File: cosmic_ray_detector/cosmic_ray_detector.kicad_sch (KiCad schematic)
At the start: 0 parts

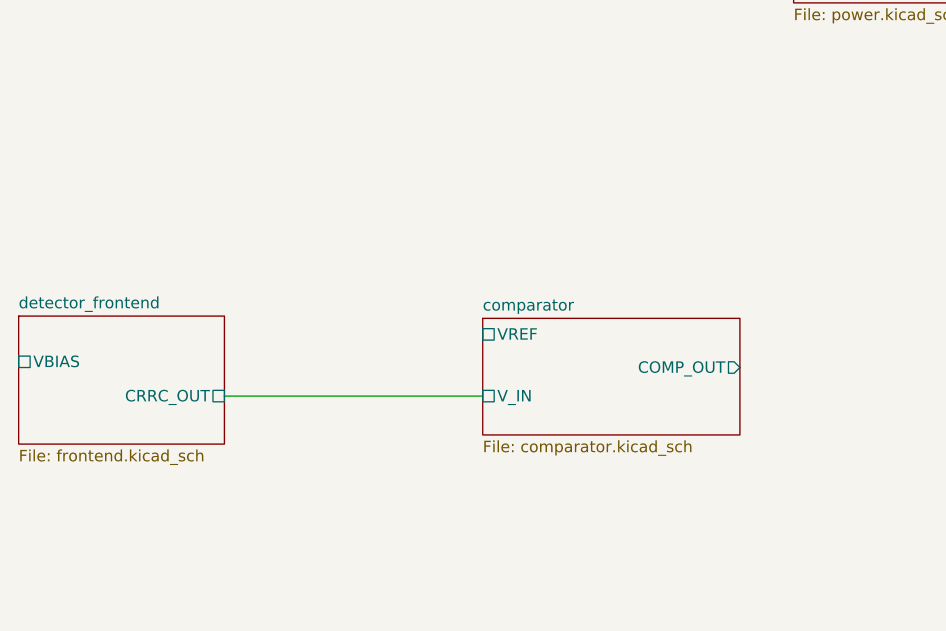
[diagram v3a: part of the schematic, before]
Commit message: schematic for threshold setting
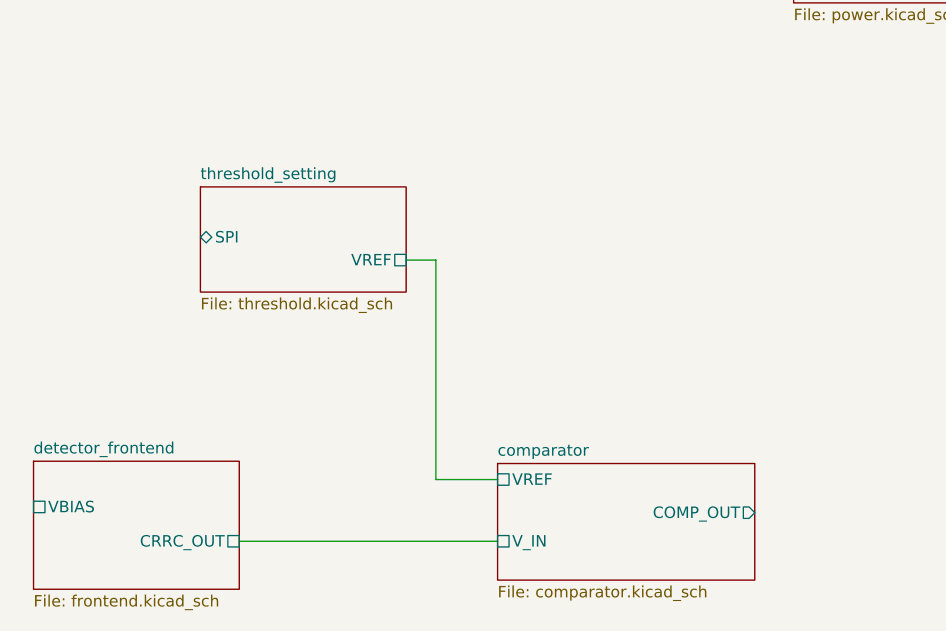
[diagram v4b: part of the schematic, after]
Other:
- added sheet threshold_setting (threshold.kicad_sch)
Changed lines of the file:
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@@
     (comment 1 "design by: Dan Weatherill")
   )
-  (wire (pts (xy 117.094 85.598) (xy 145.796 85.598))
-    (stroke (width 0) (type default) (color 0 0 0 0))
-  )
-  (sheet (at 94.234 76.708) (size 22.86 14.224) (fields_autoplaced)
-    (stroke (width 0.1524) (type solid) (color 0 0 0 0))
-    (fill (color 0 0 0 0.0000))
-    (property "Sheet name" "detector_frontend" (id 0) (at 94.234 75.9964 0)
-      (effects (font (size 1.27 1.27)) (justify left bottom))
-    )
-    (property "Sheet file" "frontend.kicad_sch" (id 1) (at 94.234 91.5166 0)
-      (effects (font (size 1.27 1.27)) (justify left top))
-    )
-    (pin "VBIAS" passive (at 94.234 81.788 180)
-      (effects (font (size 1.27 1.27)) (justify left))
-    )
-    (pin "CRRC_OUT" passive (at 117.094 85.598 0)
+  (wire (pts (xy 140.589 94.869) (xy 147.447 94.869))
+    (stroke (width 0) (type default) (color 0 0 0 0))
+  )
+  (wire (pts (xy 137.287 70.485) (xy 140.589 70.485))
+    (stroke (width 0) (type default) (color 0 0 0 0))
+  )
+  (wire (pts (xy 140.589 70.485) (xy 140.589 94.869))
+    (stroke (width 0) (type default) (color 0 0 0 0))
+  )
+  (wire (pts (xy 118.745 101.727) (xy 147.447 101.727))
+    (stroke (width 0) (type default) (color 0 0 0 0))
+  )
+  (sheet (at 114.427 62.357) (size 22.86 11.684) (fields_autoplaced)
+    (stroke (width 0.1524) (type solid) (color 0 0 0 0))
+    (fill (color 0 0 0 0.0000))
+    (property "Sheet name" "threshold_setting" (id 0) (at 114.427 61.6454 0)
+      (effects (font (size 1.27 1.27)) (justify left bottom))
+    )
+    (property "Sheet file" "threshold.kicad_sch" (id 1) (at 114.427 74.6256 0)
+      (effects (font (size 1.27 1.27)) (justify left top))
+    )
+    (pin "SPI" bidirectional (at 114.427 67.945 180)
+      (effects (font (size 1.27 1.27)) (justify left))
+    )
+    (pin "VREF" passive (at 137.287 70.485 0)
       (effects (font (size 1.27 1.27)) (justify right))
     )
   )
-  (sheet (at 145.796 76.962) (size 28.575 12.954) (fields_autoplaced)
-    (stroke (width 0.1524) (type solid) (color 0 0 0 0))
-    (fill (color 0 0 0 0.0000))
-    (property "Sheet name" "comparator" (id 0) (at 145.796 76.2504 0)
-      (effects (font (size 1.27 1.27)) (justify left bottom))
-    )
-    (property "Sheet file" "comparator.kicad_sch" (id 1) (at 145.796 90.5006 0)
-      (effects (font (size 1.27 1.27)) (justify left top))
-    )
-    (pin "V_IN" passive (at 145.796 85.598 180)
-      (effects (font (size 1.27 1.27)) (justify left))
-    )
-    (pin "VREF" passive (at 145.796 78.74 180)
-      (effects (font (size 1.27 1.27)) (justify left))
-    )
-    (pin "COMP_OUT" output (at 174.371 82.423 0)
+  (sheet (at 95.885 92.837) (size 22.86 14.224) (fields_autoplaced)
+    (stroke (width 0.1524) (type solid) (color 0 0 0 0))
+    (fill (color 0 0 0 0.0000))
+    (property "Sheet name" "detector_frontend" (id 0) (at 95.885 92.1254 0)
+      (effects (font (size 1.27 1.27)) (justify left bottom))
+    )
+    (property "Sheet file" "frontend.kicad_sch" (id 1) (at 95.885 107.6456 0)
+      (effects (font (size 1.27 1.27)) (justify left top))
+    )
+    (pin "VBIAS" passive (at 95.885 97.917 180)
+      (effects (font (size 1.27 1.27)) (justify left))
+    )
+    (pin "CRRC_OUT" passive (at 118.745 101.727 0)
+      (effects (font (size 1.27 1.27)) (justify right))
+    )
+  )
+  (sheet (at 147.447 93.091) (size 28.575 12.954) (fields_autoplaced)
+    (stroke (width 0.1524) (type solid) (color 0 0 0 0))
+    (fill (color 0 0 0 0.0000))
+    (property "Sheet name" "comparator" (id 0) (at 147.447 92.3794 0)
+      (effects (font (size 1.27 1.27)) (justify left bottom))
+    )
+    (property "Sheet file" "comparator.kicad_sch" (id 1) (at 147.447 106.6296 0)
+      (effects (font (size 1.27 1.27)) (justify left top))
+    )
+    (pin "V_IN" passive (at 147.447 101.727 180)
+      (effects (font (size 1.27 1.27)) (justify left))
+    )
+    (pin "VREF" passive (at 147.447 94.869 180)
+      (effects (font (size 1.27 1.27)) (justify left))
+    )
+    (pin "COMP_OUT" output (at 176.022 98.552 0)
       (effects (font (size 1.27 1.27)) (justify right))
     )
@@
     (path "/a7a79d2b-04f1-477d-ba1e-3ead0da72cb2" (page "3"))
     (path "/86d8b01b-5c34-47c3-904c-67d3d9a70426" (page "4"))
+    (path "/5d423df9-0691-4d6c-a6f8-df6ce27066a8" (page "5"))
   )
   (symbol_instances
@@
       (reference "#PWR?") (unit 1) (value "-5VA") (footprint "")
     )
+    (path "/5d423df9-0691-4d6c-a6f8-df6ce27066a8/14ca9c5b-ee55-4068-bbdc-0f4bbaf8a02f"
+      (reference "#PWR?") (unit 1) (value "+5VA") (footprint "")
+    )
     (path "/86d8b01b-5c34-47c3-904c-67d3d9a70426/1aa1157d-4bd6-4969-b9fb-c0b119211af2"
       (reference "#PWR?") (unit 1) (value "+5VA") (footprint "")
@@
       (reference "#PWR?") (unit 1) (value "+5VA") (footprint "")
     )
+    (path "/5d423df9-0691-4d6c-a6f8-df6ce27066a8/800bec5a-5357-4d04-8e91-1be683a70ca2"
+      (reference "#PWR?") (unit 1) (value "~") (footprint "")
+    )
+    (path "/5d423df9-0691-4d6c-a6f8-df6ce27066a8/86c8c5b0-6cb8-4805-8a1f-2a3559b19bc2"
+      (reference "#PWR?") (unit 1) (value "GNDA") (footprint "")
+    )
+    (path "/5d423df9-0691-4d6c-a6f8-df6ce27066a8/912e3c71-4816-4738-80f3-2d472a2a566a"
+      (reference "#PWR?") (unit 1) (value "GNDA") (footprint "")
+    )
     (path "/a7a79d2b-04f1-477d-ba1e-3ead0da72cb2/9655ba35-47d3-4169-b523-4be8b3cae6cb"
       (reference "#PWR?") (unit 1) (value "GNDA") (footprint "")
@@
       (reference "C?") (unit 1) (value "2.2uF") (footprint "")
     )
+    (path "/5d423df9-0691-4d6c-a6f8-df6ce27066a8/1c787f45-6ab4-410c-8c83-f15168cb7b0a"
+      (reference "C?") (unit 1) (value "1uF") (footprint "")
+    )
+    (path "/5d423df9-0691-4d6c-a6f8-df6ce27066a8/2585effe-462b-4cb2-9085-41c6b8165527"
+      (reference "C?") (unit 1) (value "10uF") (footprint "")
+    )
     (path "/6f9e921d-fe8f-4a5a-8c5c-cbe4afe99abc/352e1d1f-d8c0-4df3-82c0-73f9fc548b81"
       (reference "C?") (unit 1) (value "~") (footprint "")
@@
       (reference "C?") (unit 1) (value "10nF") (footprint "")
     )
+    (path "/5d423df9-0691-4d6c-a6f8-df6ce27066a8/4c8c9d10-0592-4577-9dfa-2a99d989669b"
+      (reference "C?") (unit 1) (value "0.1uF") (footprint "")
+    )
     (path "/6f9e921d-fe8f-4a5a-8c5c-cbe4afe99abc/64d6d08c-f5e1-413e-9e3e-c0a6aeb2fc5f"
       (reference "C?") (unit 1) (value "C") (footprint "")
@@
       (reference "D?") (unit 1) (value "12V") (footprint "Diode_SMD:D_SOD-123")
     )
+    (path "/5d423df9-0691-4d6c-a6f8-df6ce27066a8/65278bfc-14d1-478b-8143-85b3c07e62c3"
+      (reference "IC?") (unit 1) (value "AD5270BRMZ-100-RL7") (footprint "SOP50P490X110-10N")
+    )
     (path "/86d8b01b-5c34-47c3-904c-67d3d9a70426/af3aa5f2-62c8-4412-beae-b6c8e5ade3ec"
       (reference "IC?") (unit 1) (value "TLV3501AIDBVTG4") (footprint "SOT95P280X145-6N")
     )
+    (path "/5d423df9-0691-4d6c-a6f8-df6ce27066a8/186fe6f1-8e1f-4ed0-94da-2735e4d5402a"
+      (reference "R?") (unit 1) (value "R_US") (footprint "")
+    )
     (path "/a7a79d2b-04f1-477d-ba1e-3ead0da72cb2/2a7929ff-9f40-4bd1-bcfb-e606c3c4db50"

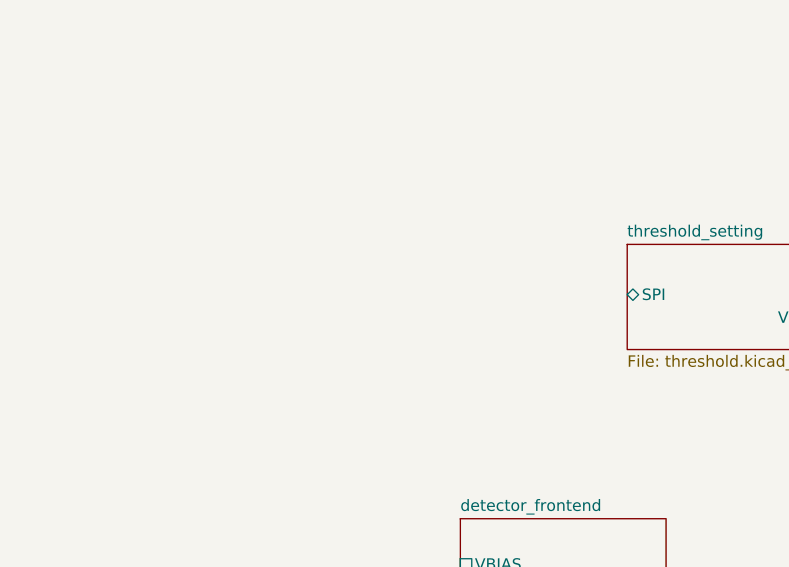
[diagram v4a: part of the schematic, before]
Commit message: add some net labels to frontends
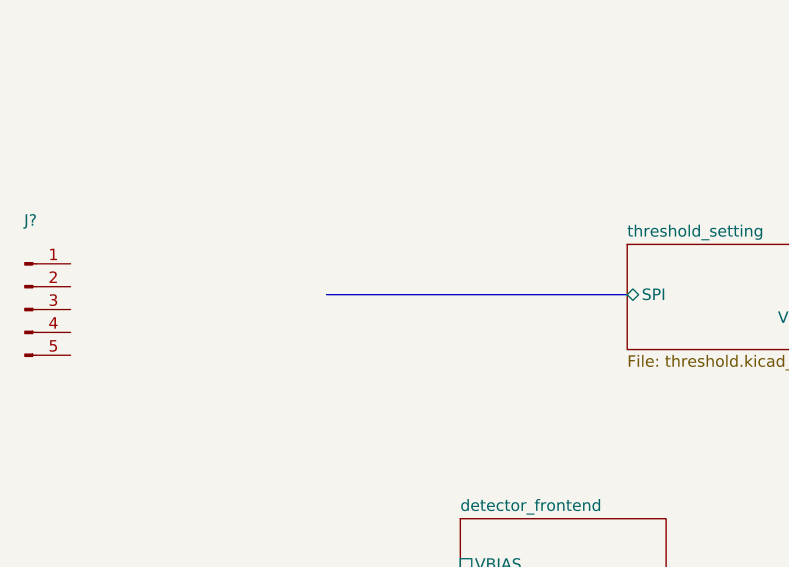
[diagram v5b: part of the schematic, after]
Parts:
- added J?: (no value), symbol Connector:Conn_01x05_Male
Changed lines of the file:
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@@
     (stroke (width 0) (type default) (color 0 0 0 0))
+  )
+  (bus (pts (xy 81.026 67.945) (xy 114.427 67.945))
+    (stroke (width 0) (type default) (color 0 0 0 0))
+  )
+  (symbol (lib_id "Connector:Conn_01x05_Male") (at 47.498 69.596 0) (unit 1)
+    (in_bom yes) (on_board yes) (fields_autoplaced)
+    (property "Reference" "J?" (id 0) (at 48.133 59.69 0))
+    (property "Value" "" (id 1) (at 48.133 62.23 0))
+    (property "Footprint" "" (id 2) (at 47.498 69.596 0)
+      (effects (font (size 1.27 1.27)) hide)
+    )
+    (property "Datasheet" "~" (id 3) (at 47.498 69.596 0)
+      (effects (font (size 1.27 1.27)) hide)
+    )
+    (pin "1")
+    (pin "2")
+    (pin "3")
+    (pin "4")
+    (pin "5")
   )
   (sheet (at 114.427 62.357) (size 22.86 11.684) (fields_autoplaced)
@@
       (reference "IC?") (unit 1) (value "TLV3501AIDBVTG4") (footprint "SOT95P280X145-6N")
     )
+    (path "/24fd848e-66f1-47e7-9f72-61ad17d16c83"
+      (reference "J?") (unit 1) (value "Conn_01x05_Male") (footprint "")
+    )
     (path "/5d423df9-0691-4d6c-a6f8-df6ce27066a8/186fe6f1-8e1f-4ed0-94da-2735e4d5402a"

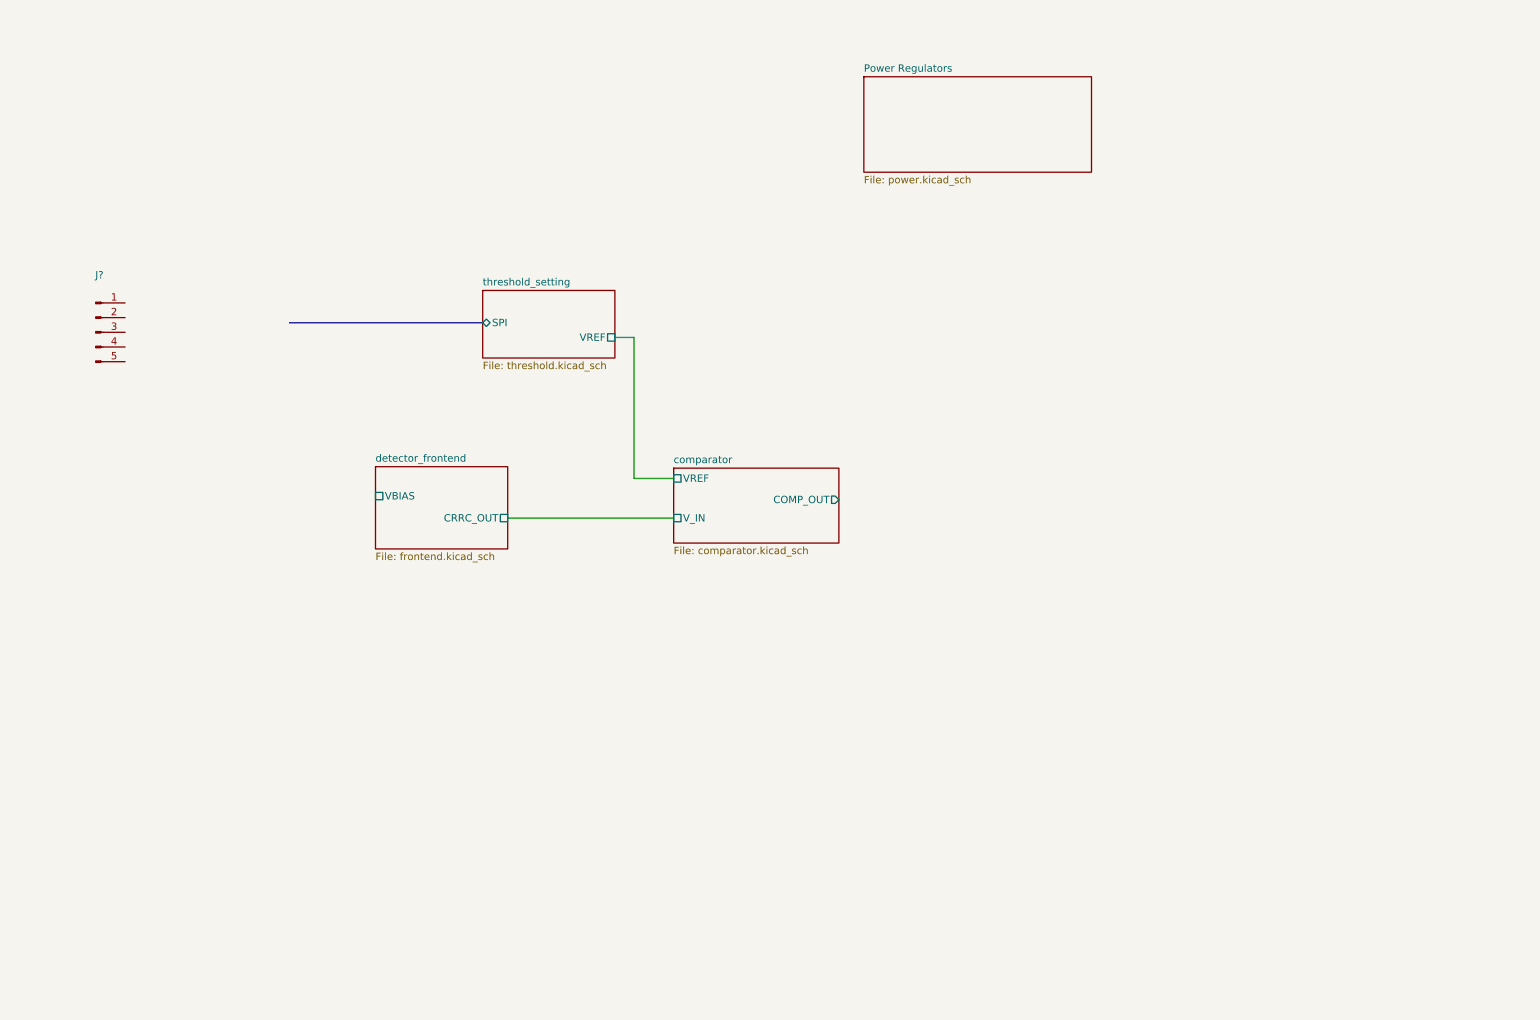
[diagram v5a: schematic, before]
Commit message: roughly finished schematic ready for annotation & ERC
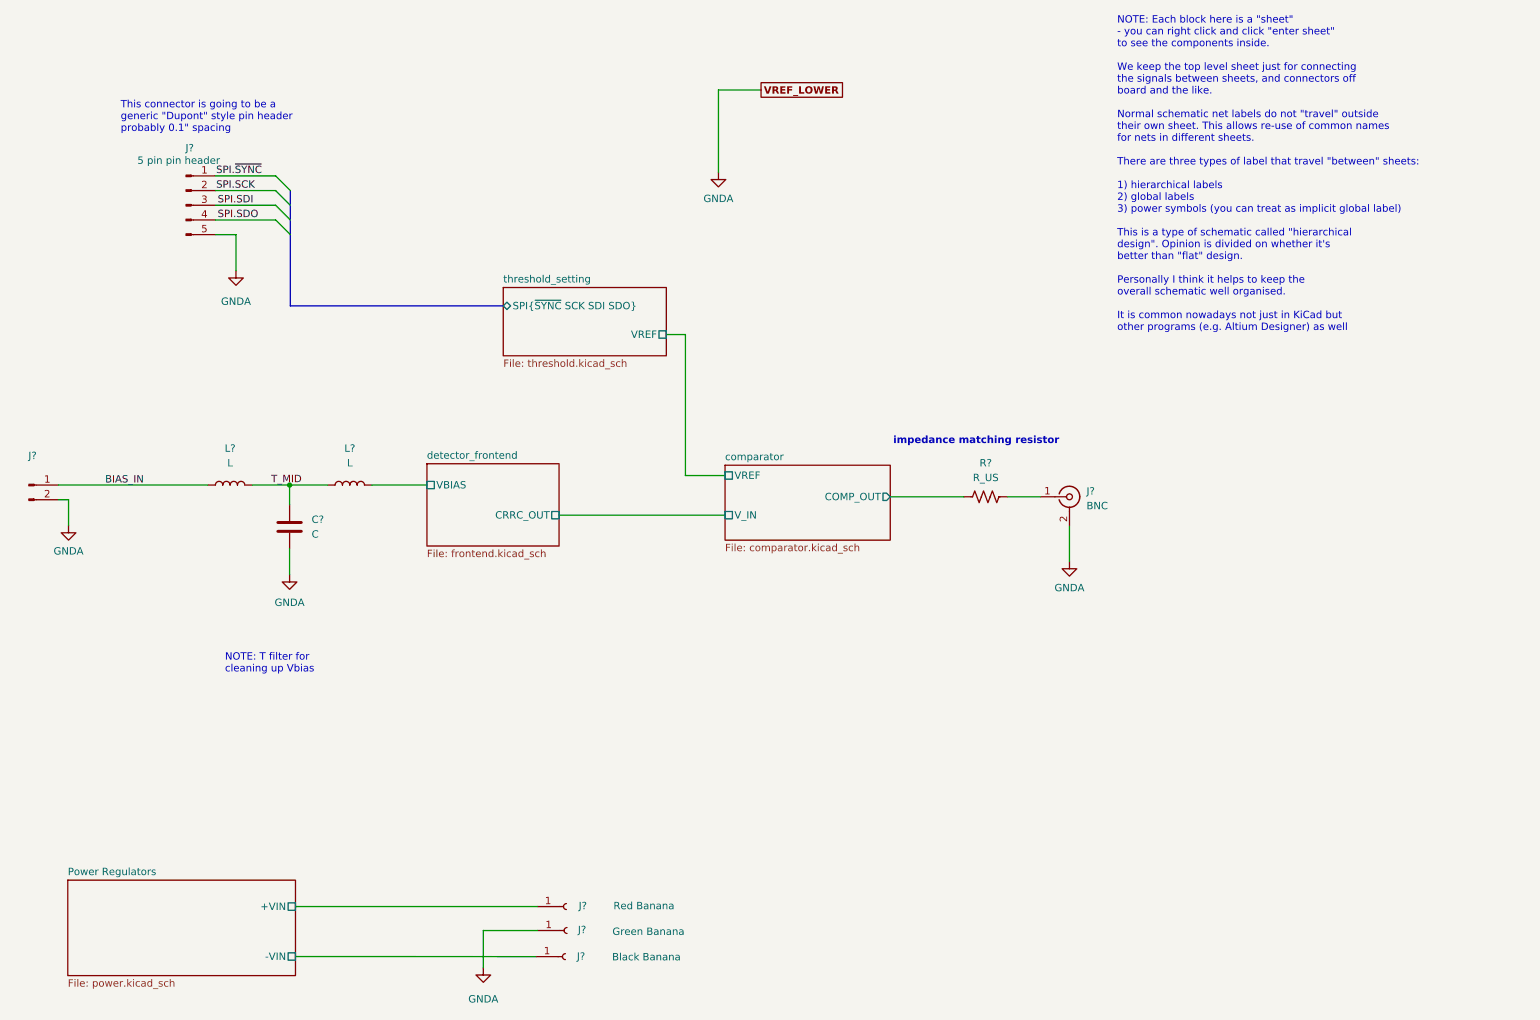
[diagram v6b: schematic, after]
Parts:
- added C?: C, symbol Device:C
- added J?: BNC, symbol Connector:Conn_Coaxial
- added J?: Red Banana, symbol Connector:Conn_01x01_Female
- added J?: (no value), symbol Connector:Conn_01x02_Male
- added J?: Green Banana, symbol Connector:Conn_01x01_Female
- added J?: Black Banana, symbol Connector:Conn_01x01_Female
- added L? (x2): L, symbol Device:L
- added R?: R_US, symbol Device:R_US
- J?: value (none) -> 5 pin pin header
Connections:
- net comparator/COMP_OUT: now also R?.1
- net detector_frontend/VBIAS: now also L?.2
- net SPI.~{SYNC}: now reaches J?.1 (Pin_1)
- net SPI.SCK: now reaches J?.2 (Pin_2)
- net SPI.SDI: now reaches J?.3 (Pin_3)
- net SPI.SDO: now reaches J?.4 (Pin_4)
- net GNDA: now reaches J?.5 (Pin_5)
- net GNDA: now also C?.1, J?.1 (Pin_1), J?.2 (Ext), J?.2 (Pin_2)
- new net: J?.1 (In), R?.2
- new net: J?.1 (Pin_1), L?.1
- new net Power Regulators/+VIN: J?.1 (Pin_1)
- new net Power Regulators/-VIN: J?.1 (Pin_1)
- new net T_MID: C?.2, L?.1, L?.2
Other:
- sheet Power Regulators ports: added +VIN, -VIN; removed none
- sheet threshold_setting ports: added SPI{~{SYNC} SCK SDI SDO}; removed SPI
- note added: "NOTE: Each block here is a "sheet" - you can right click and click "enter sheet" to see the components inside. We keep the top level sheet just for connecting the signals between sheets, and connectors off board and the like. Normal schematic net labels do not "travel" outside their own sheet. This allows re-use of common names for nets in different sheets. There are three types of label that tra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"
- note added: "NOTE: T filter for cleaning up Vbias"
- note added: "This connector is going to be a generic "Dupont" style pin header probably 0.1" spacing"
- note added: "impedance matching resistor"
- moved on the sheet: J?

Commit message: annotated schematic
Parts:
- gave numbers to parts that had none: 10
